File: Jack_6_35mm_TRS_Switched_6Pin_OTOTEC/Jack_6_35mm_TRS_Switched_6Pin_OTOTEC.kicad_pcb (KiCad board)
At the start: 2 copper layers, 1 part

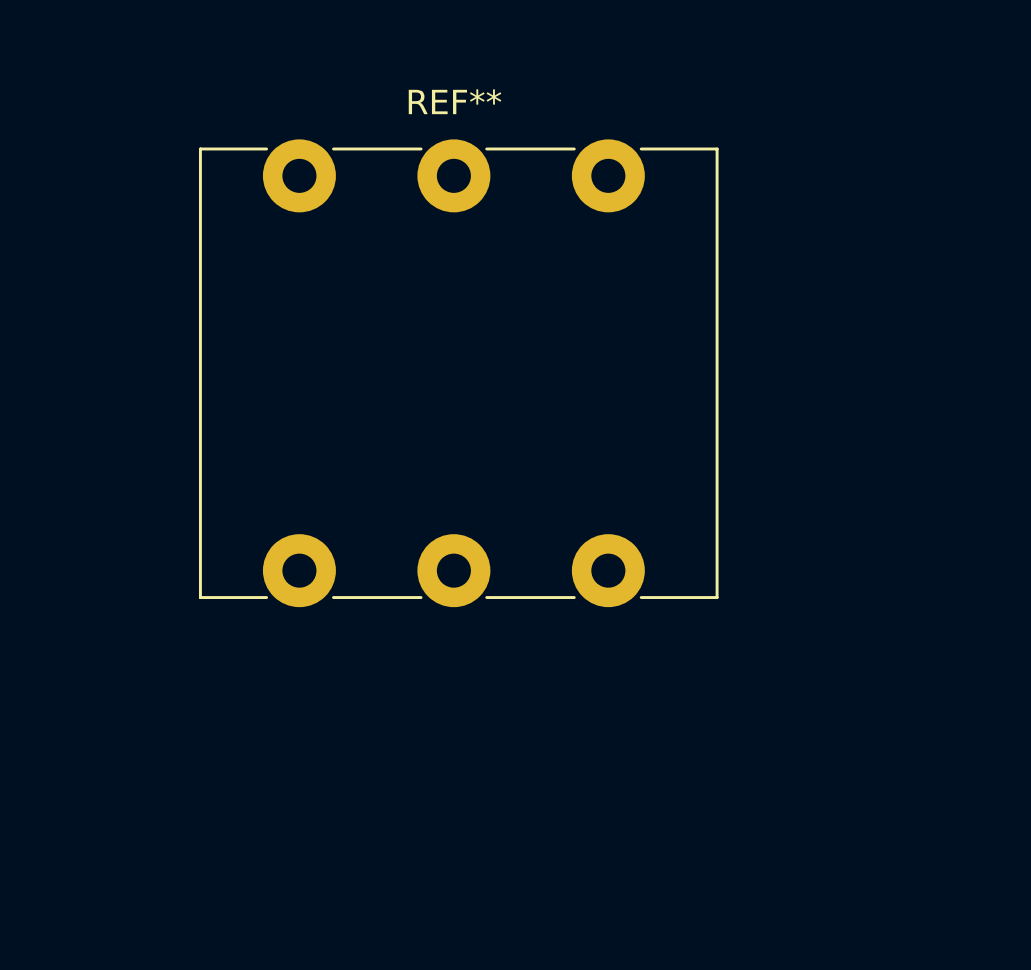
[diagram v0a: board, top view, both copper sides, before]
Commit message: feat: finish first working jack breakout PCB
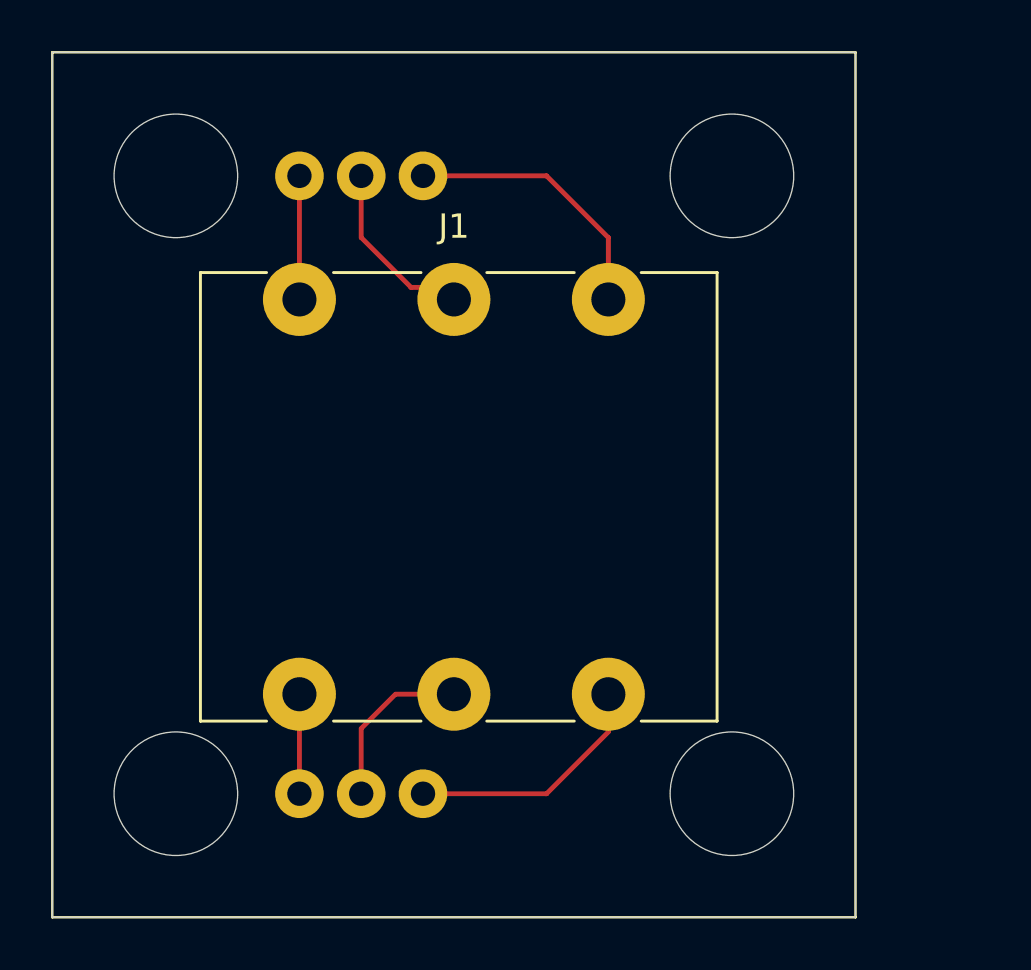
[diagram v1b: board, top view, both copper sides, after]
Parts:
- removed REF**: Jack_6.35mm_OTOTEC_TRS_Switched_6Pin, OTOTEC:Jack_6.35mm_OTOTEC_TRS_Switched_6Pin
- added ?: , , F.Cu at (30.5, 45.7)
- added ?: , , F.Cu at (27.9, 45.7)
- added ?: , , F.Cu at (27.9, 20.3)
- added ?: , , F.Cu at (25.4, 20.3)
- added ?: , , F.Cu at (25.4, 45.7)
- added ?: , , F.Cu at (30.5, 20.3)
- added J1: NMJ6HCD2, OTOTEC:Jack_6.35mm_OTOTEC_TRS_Switched_6Pin, F.Cu at (25.4, 25.4)
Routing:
- net unconnected-(J1-PadS): track 0.00 -> 11.2 mm
- net unconnected-(J1-PadSN): track 0.00 -> 10.2 mm
- net unconnected-(J1-PadR): track 0.00 -> 7.69 mm
- net unconnected-(J1-PadRN): track 0.00 -> 7.07 mm
- net unconnected-(J1-PadT): track 0.00 -> 5.08 mm
- net unconnected-(J1-PadTN): track 0.00 -> 4.09 mm
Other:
- board outline added: 33 x 35.6 mm

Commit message: feat: improve breadboard connectivity
- Added 3-pin headers for easier breadboard connection
- Added proper schematic connections and net routing
- Improved PCB layout with rounded corners
- Added project metadata and schematic title
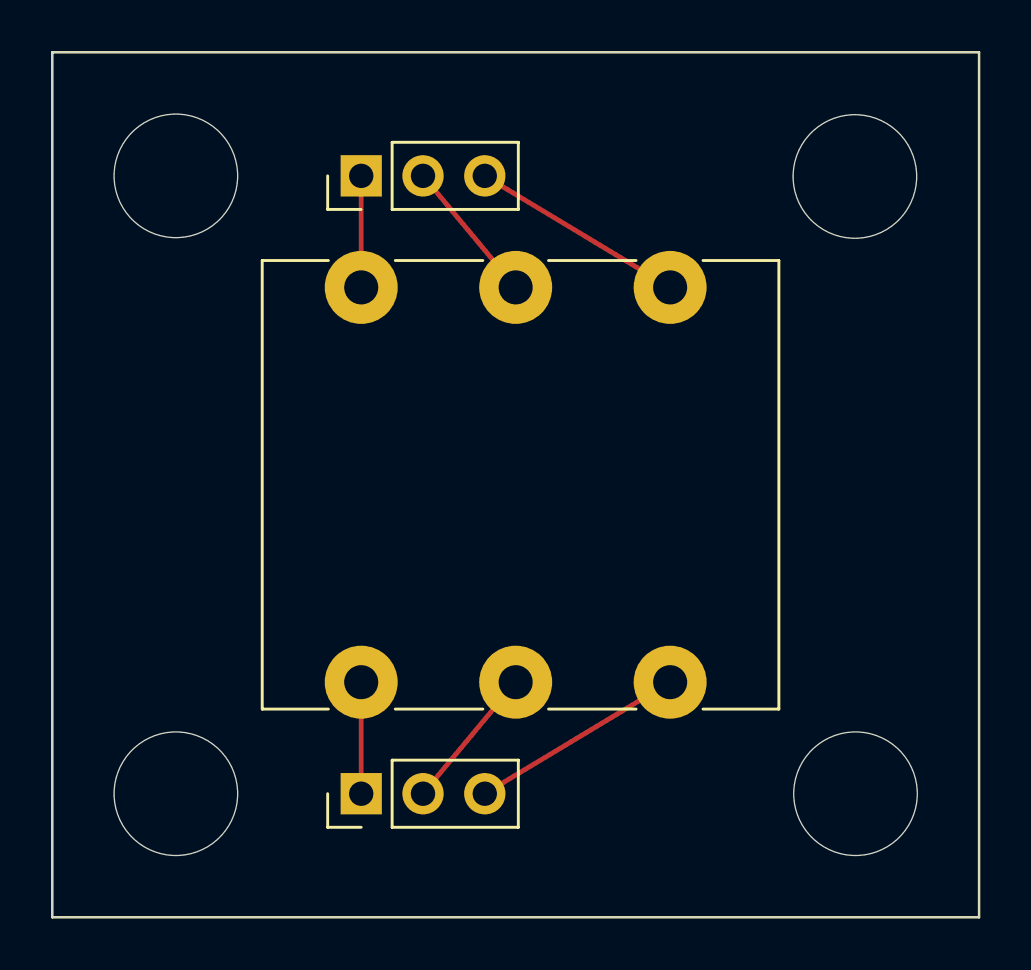
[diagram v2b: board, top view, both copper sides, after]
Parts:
- removed ? (x6): , 
- added Conn_01x03_Pin1: TRS_NORMAL, Connector_PinHeader_2.54mm:PinHeader_1x03_P2.54mm_Vertical, F.Cu at (27.9, 45.7)
- added Conn_01x03_Pin2: TRS, Connector_PinHeader_2.54mm:PinHeader_1x03_P2.54mm_Vertical, F.Cu at (27.9, 20.3)
- moved J1 2.59 mm to (27.9, 24.9)
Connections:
- J1 pad R: unconnected-(J1-PadR) -> Net-(Conn_01x03_Pin2-Pin_2)
- J1 pad RN: unconnected-(J1-PadRN) -> Net-(Conn_01x03_Pin1-Pin_2)
- J1 pad S: unconnected-(J1-PadS) -> Net-(Conn_01x03_Pin2-Pin_3)
- J1 pad SN: unconnected-(J1-PadSN) -> Net-(Conn_01x03_Pin1-Pin_3)
- J1 pad T: unconnected-(J1-PadT) -> Net-(Conn_01x03_Pin2-Pin_1)
- J1 pad TN: unconnected-(J1-PadTN) -> Net-(Conn_01x03_Pin1-Pin_1)
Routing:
- net unconnected-(J1-PadS): track 11.2 -> 0.00 mm
- net unconnected-(J1-PadSN): track 10.2 -> 0.00 mm
- net Net-(Conn_01x03_Pin2-Pin_3): track 0.00 -> 8.89 mm
- net Net-(Conn_01x03_Pin1-Pin_3): track 0.00 -> 8.89 mm
- net unconnected-(J1-PadR): track 7.69 -> 0.00 mm
- net unconnected-(J1-PadRN): track 7.07 -> 0.00 mm
- net Net-(Conn_01x03_Pin2-Pin_2): track 0.00 -> 5.96 mm
- net Net-(Conn_01x03_Pin1-Pin_2): track 0.00 -> 5.96 mm
- net unconnected-(J1-PadT): track 5.08 -> 0.00 mm
- net Net-(Conn_01x03_Pin2-Pin_1): track 0.00 -> 4.59 mm
- net Net-(Conn_01x03_Pin1-Pin_1): track 0.00 -> 4.59 mm
- net unconnected-(J1-PadTN): track 4.09 -> 0.00 mm
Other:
- board size 33 x 35.6 mm -> 38.1 x 35.6 mm

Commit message: feat: finalize TRS breadboard adapter Rev 1
- Increase signal trace width to 0.8 mm
- Add TRS and switched-contact pin labels
- Add jack orientation marker
- Add artwork and silkscreen details;
- Add AJDB logo footprint
- Add project identification and repository information
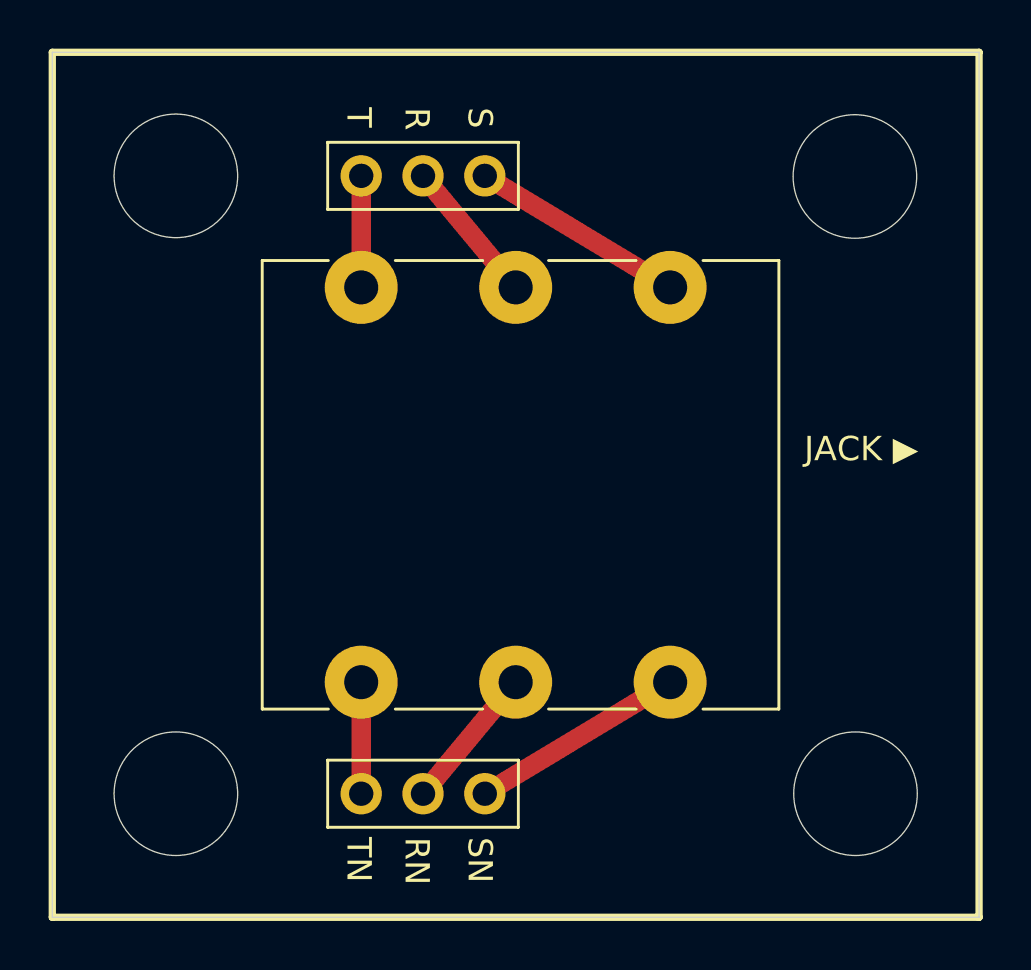
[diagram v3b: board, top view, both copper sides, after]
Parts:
- added REF**: ajdb-devil-balloon-logo, AJDB:ajdb-devil-balloon-logo, B.Cu at (34.3, 33.0)
- Conn_01x03_Pin1, Conn_01x03_Pin2: footprint Connector_PinHeader_2.54mm:PinHeader_1x03_P2.54mm_Vertical -> OTOTEC:PinHeader_1x03_P2.54mm_Vertical
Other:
- board text added: "JACK ▶"
- board text added: "R"
- board text added: "RN"
- board text added: "S"
- board text added: "SN"
- board text added: "T"
- board text added: "TN"
- board text added: "TRS Breadboard Adapter • Rev 1"
- board text added: "github.com/CurtesMalteser"
